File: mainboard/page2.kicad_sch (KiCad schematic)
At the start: 37 parts, among them IC1 TCAN3414DR, J10 XT30U-M, J11 XT30U-M, J12 Conn_01x03, J13 BM02B-SRSS-TB, J14 BM02B-SRSS-TB, J15 BM02B-SRSS-TB, J16 BM04B-SRSS-TB, J17 BM04B-SRSS-TB, J18 BM04B-SRSS-TB, J19 BM04B-SRSS-TB, J20 BM04B-SRSS-TB, J23 Conn_02x04_Odd_Even, J24 BM02B-SRSS-TB, J25 BM02B-SRSS-TB, J26 BM02B-SRSS-TB, J6 XT30U_M, J7 XT30U-M, J8 XT30U-M, J9 XT30U-M, U3 TCA9548APWR

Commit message: started work on mainboard
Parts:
- removed C7: 0.1uF, Capacitor_SMD:C_0805_2012Metric_Pad1.18x1.45mm_HandSolder, symbol Device:C
- removed J17, J18, J19: BM04B-SRSS-TB, Connector_JST:JST_SH_BM04B-SRSS-TB_1x04-1MP_P1.00mm_Vertical, symbol QWIIC:PRT-14417
- removed R17, R18, R19, R20, R21, R22: 4.7K, Resistor_SMD:R_0805_2012Metric_Pad1.20x1.40mm_HandSolder, symbol Device:R_US
- removed R23: 10K, Resistor_SMD:R_0805_2012Metric_Pad1.20x1.40mm_HandSolder, symbol Device:R_US
- removed U3: TCA9548APWR, Package_SO:TSSOP-24_4.4x7.8mm_P0.65mm, symbol Interface_Expansion:TCA9548APWR
- J13, J14, J15, J24, J25, J26: value BM02B-SRSS-TB -> B2B-PH-K; footprint Connector_JST:JST_SH_BM02B-SRSS-TB_1x02-1MP_P1.00mm_Vertical -> Connector_JST:JST_PH_B2B-PH-K_1x02_P2.00mm_Vertical
- J23: value Conn_02x04_Odd_Even -> Jertson Header; symbol Connector_Generic:Conn_02x04_Odd_Even -> Connector_Generic:Conn_02x20_Odd_Even
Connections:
- net GND: now also J23.14 (Pin_14), J23.20 (Pin_20), J23.25 (Pin_25), J23.30 (Pin_30), J23.34 (Pin_34), J23.39 (Pin_39), J23.9 (Pin_9)
- net GPIO_GCLK: no longer J23.7 (Pin_7)
- net SCLS0 renamed SCL0
- net SCL0: now also J23.28 (Pin_28)
- net SDAS0 renamed SDA0
- net SDA0: now also J23.27 (Pin_27)
- no-connect marks 12 -> 28
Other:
- note added: "NOT ETHERNET (100% sure)"
- note removed: "I2C MultiPlex"
- note removed: "NOT ETHERNET"
- note removed: "Reset pin may change later"
- moved on the sheet: C14, C16, IC1, J16, J20, R15, R16, R24, R25, R26, R3

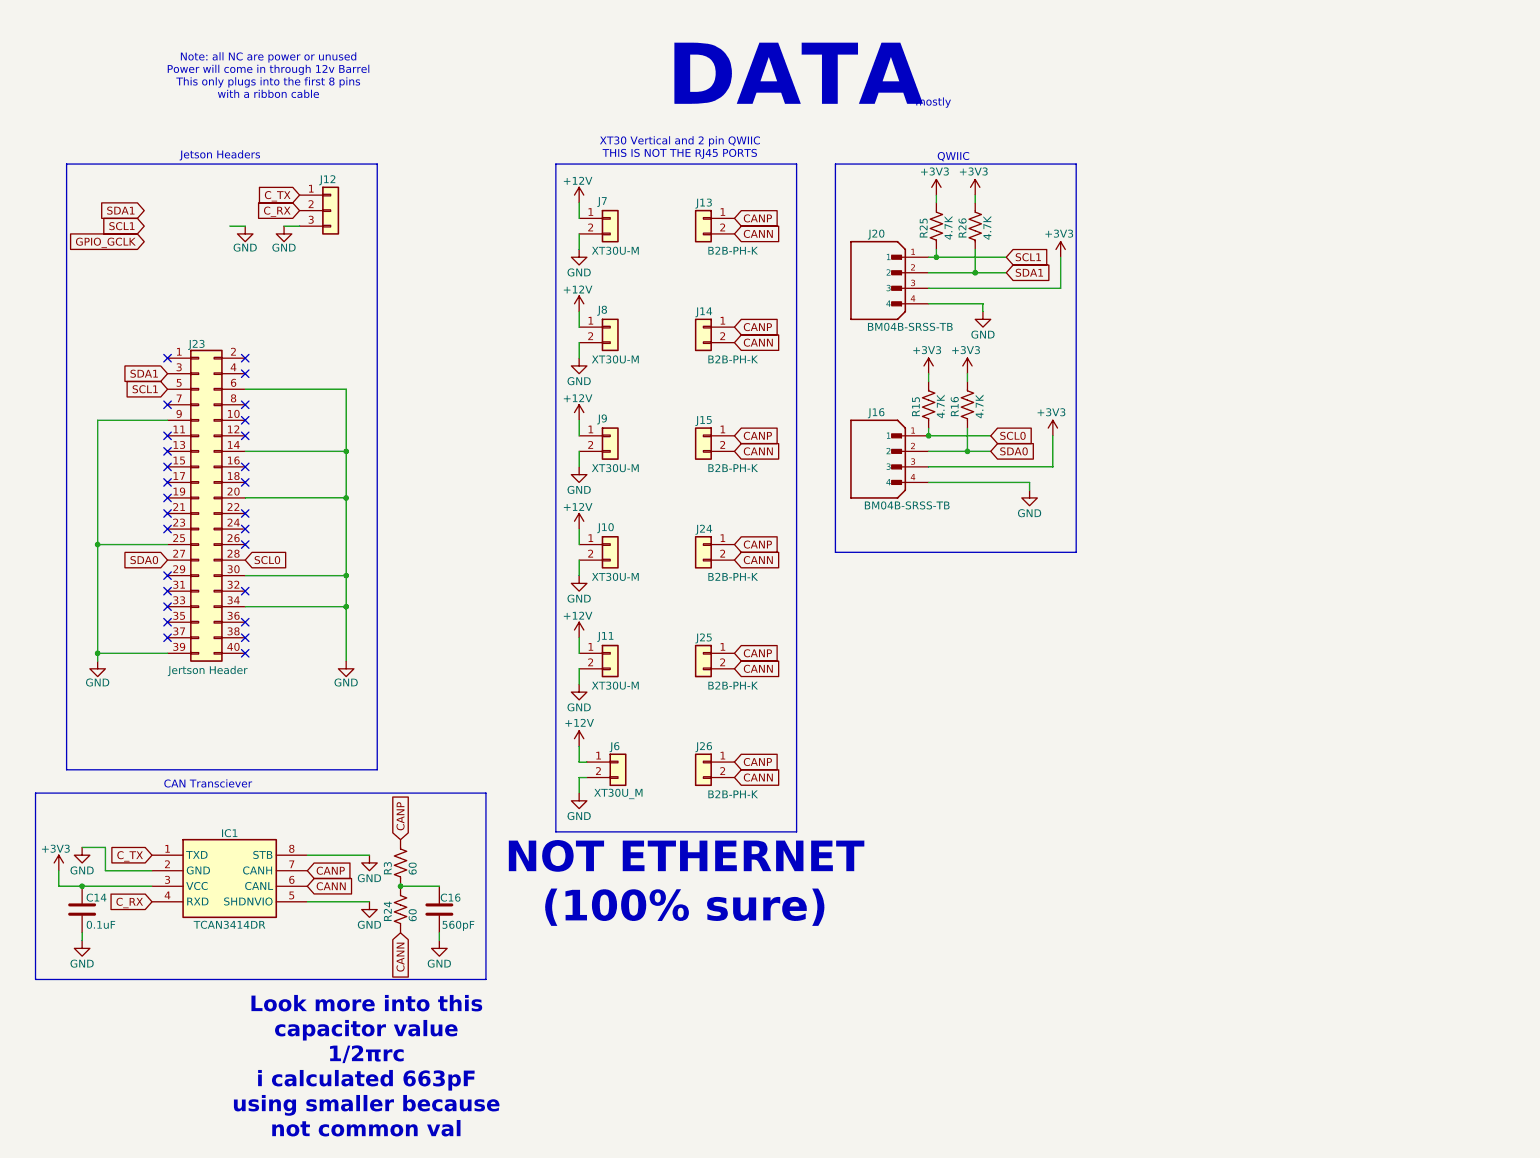
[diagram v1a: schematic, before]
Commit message: layed out PCB, started routing of mainboard
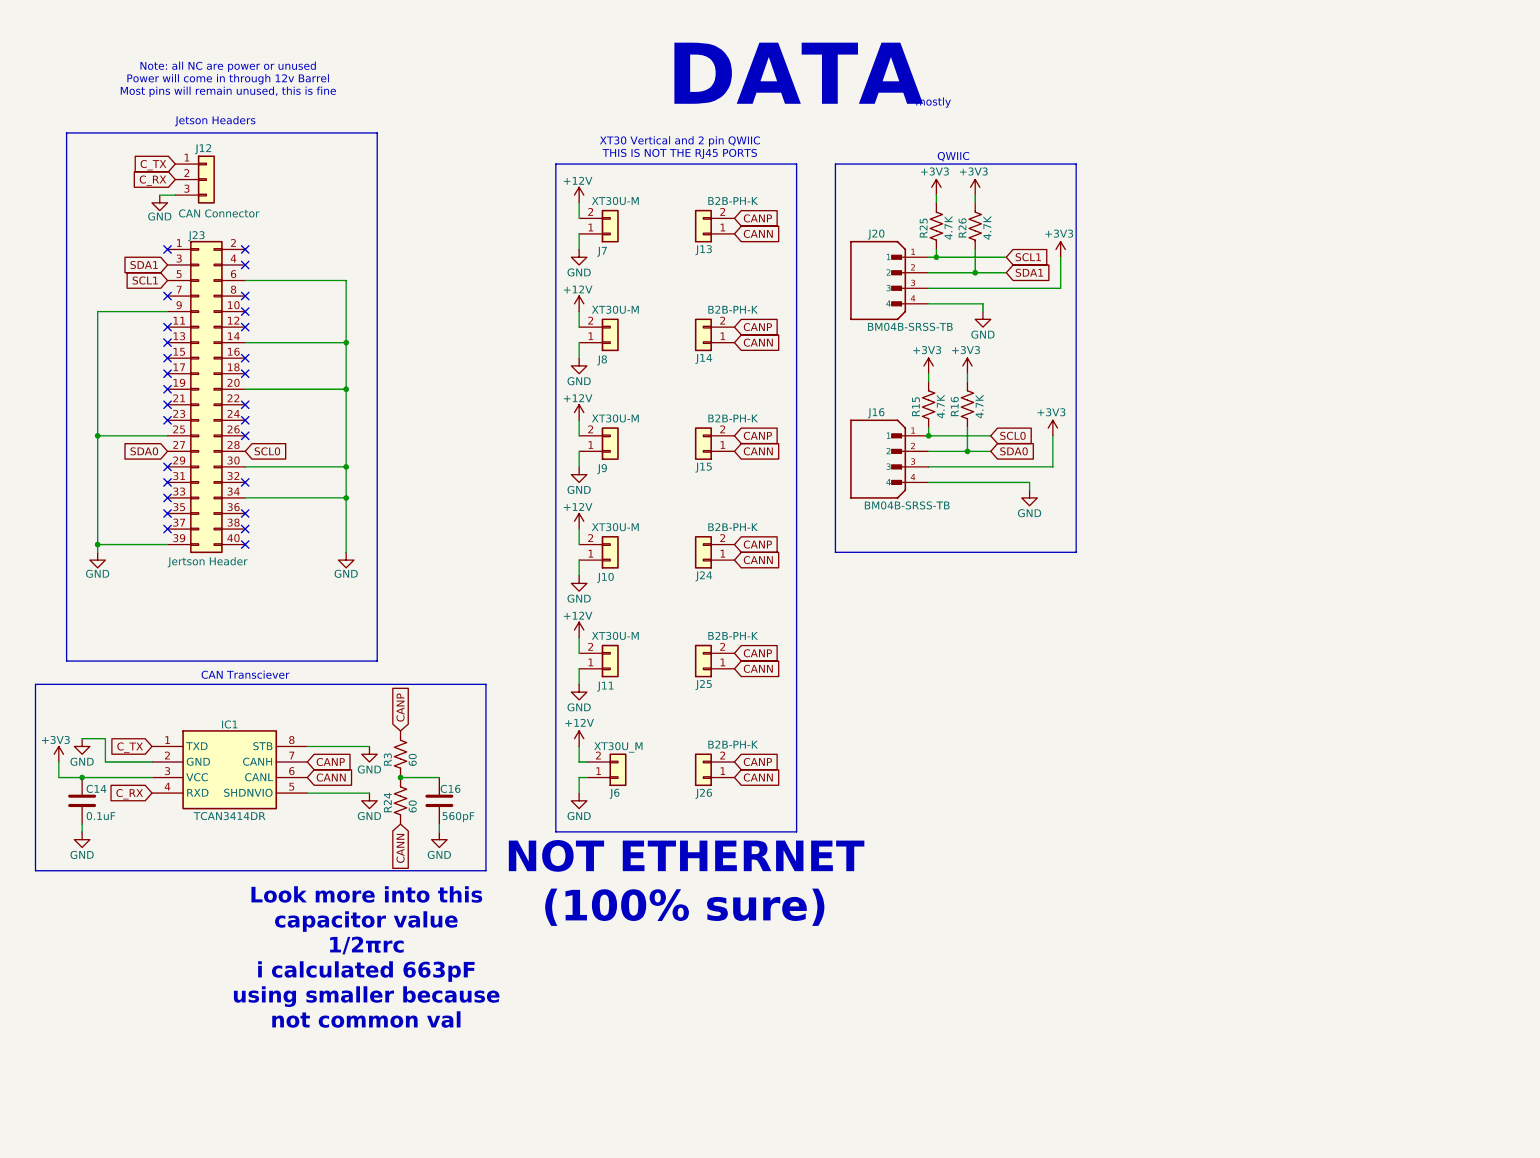
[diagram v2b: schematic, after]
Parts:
- J12: value Conn_01x03 -> CAN Connector
- J23: footprint Connector_PinHeader_2.54mm:PinHeader_2x04_P2.54mm_Vertical -> Connector_PinHeader_2.54mm:PinHeader_2x20_P2.54mm_Vertical
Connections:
- net +12V: now also J10.2 (Pin_2), J11.2 (Pin_2), J6.2 (Pin_2), J7.2 (Pin_2), J8.2 (Pin_2), J9.2 (Pin_2); no longer J10.1 (Pin_1), J11.1 (Pin_1), J6.1 (Pin_1), J7.1 (Pin_1), J8.1 (Pin_1), J9.1 (Pin_1)
- net CANN: now also J13.1 (Pin_1), J14.1 (Pin_1), J15.1 (Pin_1), J24.1 (Pin_1), J25.1 (Pin_1), J26.1 (Pin_1); no longer J13.2 (Pin_2), J14.2 (Pin_2), J15.2 (Pin_2), J24.2 (Pin_2), J25.2 (Pin_2), J26.2 (Pin_2)
- net CANP: now also J13.2 (Pin_2), J14.2 (Pin_2), J15.2 (Pin_2), J24.2 (Pin_2), J25.2 (Pin_2), J26.2 (Pin_2); no longer J13.1 (Pin_1), J14.1 (Pin_1), J15.1 (Pin_1), J24.1 (Pin_1), J25.1 (Pin_1), J26.1 (Pin_1)
- net GND: now also J10.1 (Pin_1), J11.1 (Pin_1), J6.1 (Pin_1), J7.1 (Pin_1), J8.1 (Pin_1), J9.1 (Pin_1); no longer J10.2 (Pin_2), J11.2 (Pin_2), J6.2 (Pin_2), J7.2 (Pin_2), J8.2 (Pin_2), J9.2 (Pin_2)
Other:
- note added: "Note: all NC are power or unused Power will come in through 12v Barrel Most pins will remain unused, this is fine"
- note removed: "Note: all NC are power or unused Power will come in through 12v Barrel This only plugs into the first 8 pins with a ribbon cable"
- title: Main Board 2024-2025 -> Main Board 2025-2026
- moved on the sheet: C14, C16, IC1, J12, J13, J14, J15, J23, J24, J25, J26, R24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

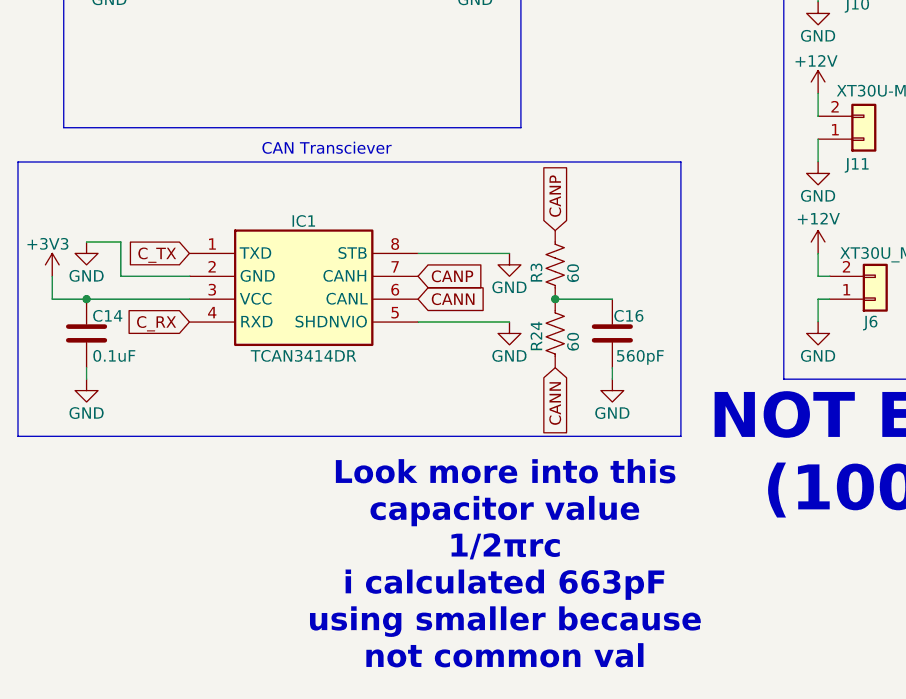
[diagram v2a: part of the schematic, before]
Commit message: added tvs diode to baord (this was sylvester not nitin)
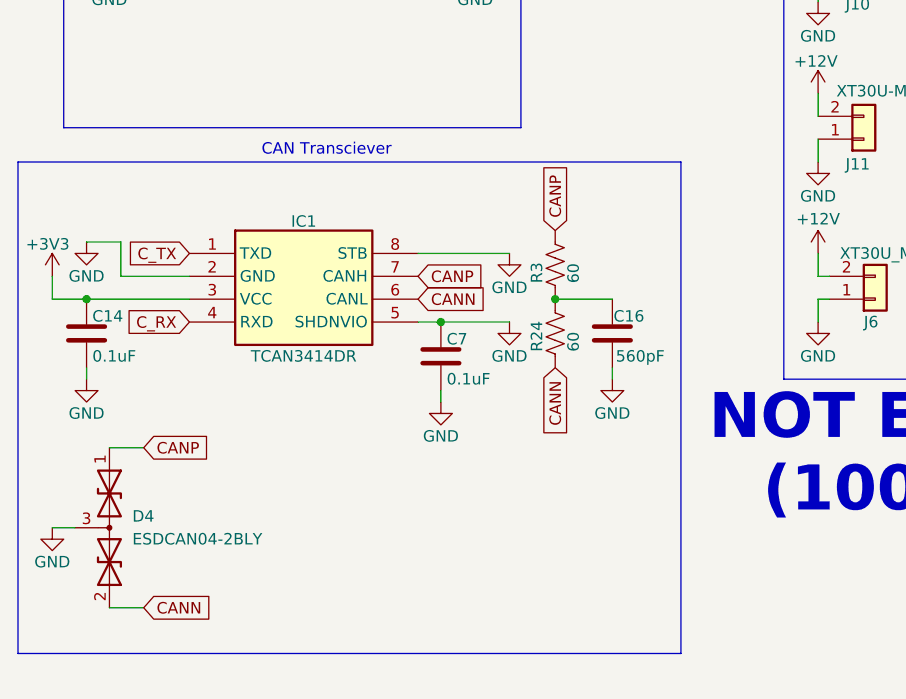
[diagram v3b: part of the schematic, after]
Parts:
- added C7: 0.1uF, Capacitor_SMD:C_0805_2012Metric_Pad1.18x1.45mm_HandSolder, symbol Device:C
- added D4: ESDCAN04-2BLY, Package_TO_SOT_SMD:TSOT-23_HandSoldering, symbol Device:D_TVS_Dual_AAC
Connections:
- net CANN: now also D4.2 (A2)
- net CANP: now also D4.1 (A1)
- net GND: now also C7.1, C7.2, D4.3 (common)
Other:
- note removed: "Look more into this capacitor value 1/2πrc i calculated 663pF using smaller because not common val"
